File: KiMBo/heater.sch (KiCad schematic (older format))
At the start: 61 parts, among them Q10 2N7002, Q11 2N7002, Q12 DMP3098L-7, Q13 DMP3098L-7, Q4 2N7002, Q5 IPD90P03P4-04, Q6 2N7002, Q7 2N7002, Q8 DMP3098L-7, Q9 DMP3098L-7

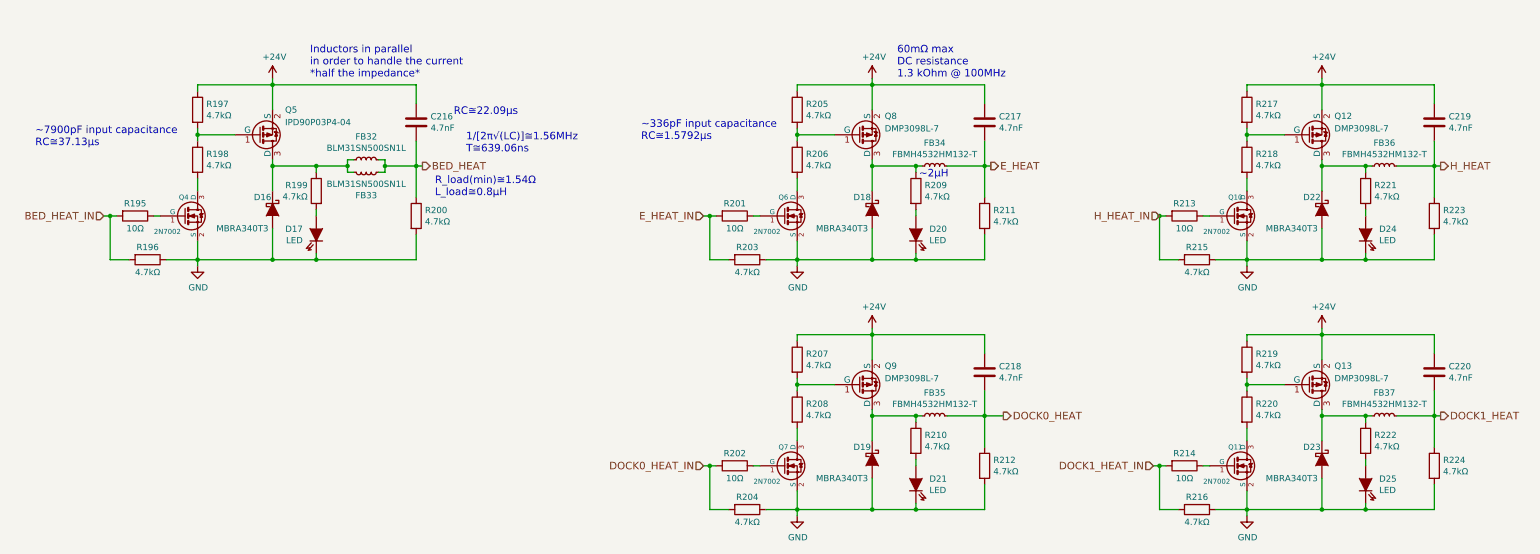
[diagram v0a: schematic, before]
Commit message: Connect X and Z stepper driver open-drain DIAG0 and DIAG1 lines together
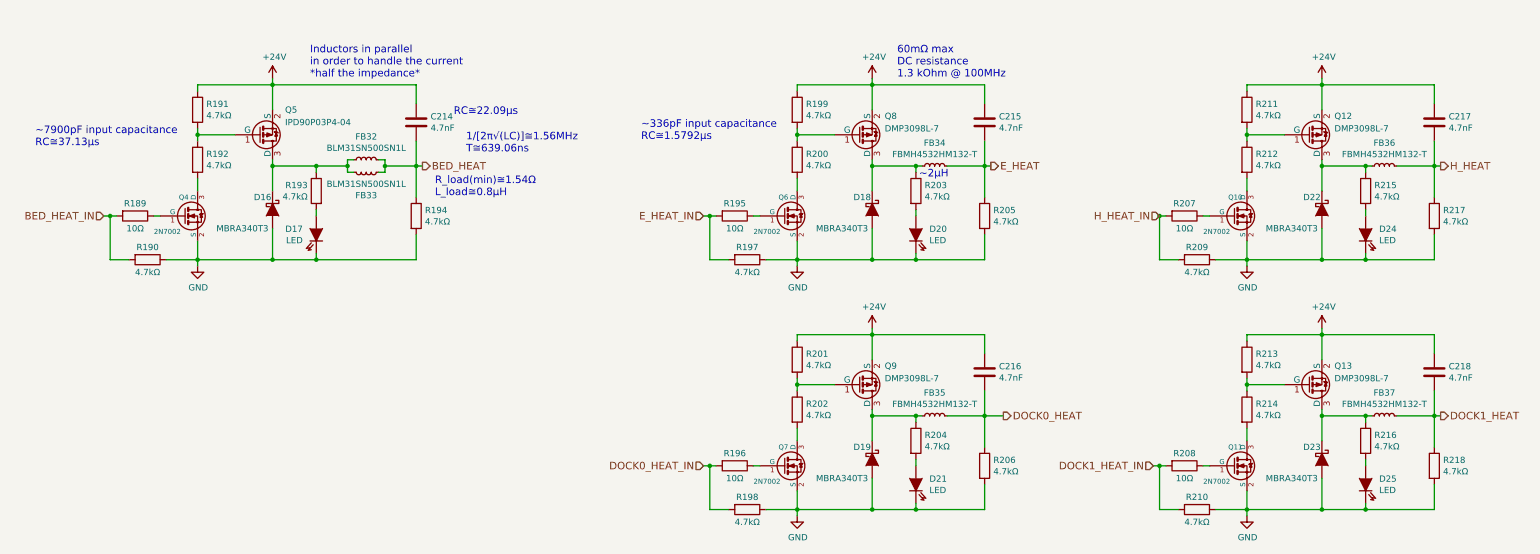
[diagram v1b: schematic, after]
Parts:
- renumbered C216 to C214, C217 to C215, C218 to C216, C219 to C217, C220 to C218, R195 to R189, R196 to R190, R197 to R191, R198 to R192, R199 to R193, R200 to R194, R201 to R195, R202 to R196, R203 to R197, R204 to R198, R205 to R199, R206 to R200, R207 to R201, R208 to R202, R209 to R203, R210 to R204, R211 to R205, R212 to R206, R213 to R207, R214 to R208, R215 to R209, R216 to R210, R217 to R211, R218 to R212, R219 to R213, R220 to R214, R221 to R215, R222 to R216, R223 to R217, R224 to R218

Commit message: Leave SPI0 free for a display, reassign pins so SPI1 is available
Fix some typos/errors
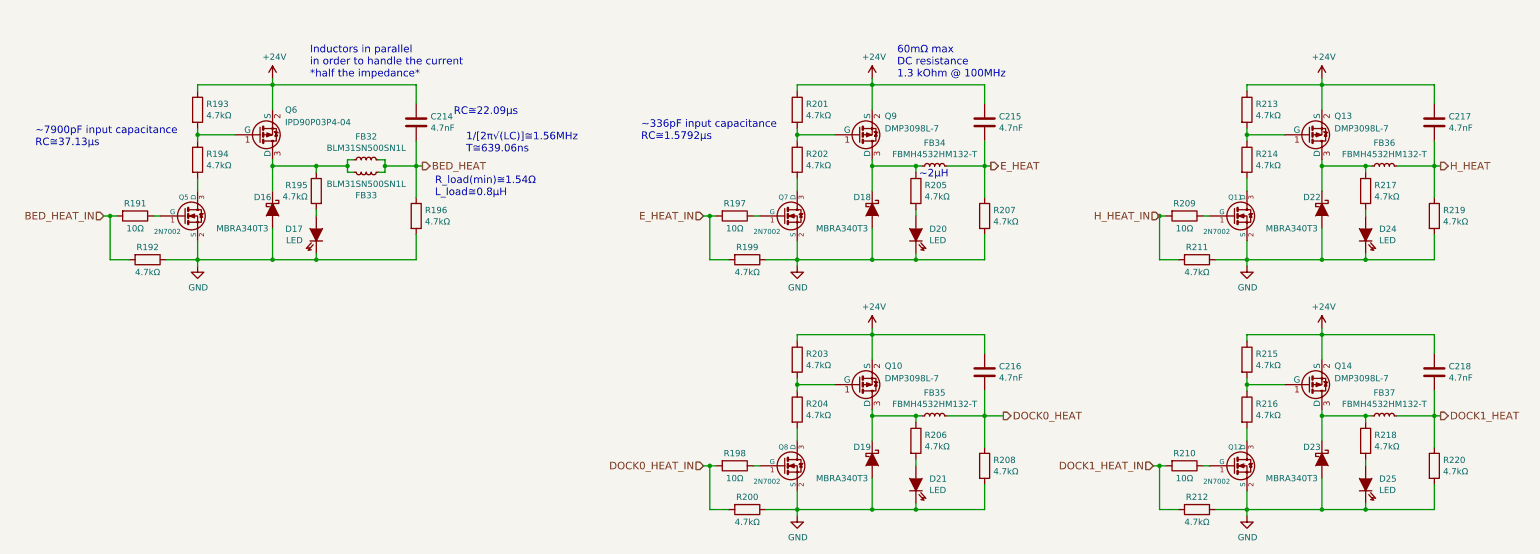
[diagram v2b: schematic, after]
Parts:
- renumbered Q9 to Q10, Q10 to Q11, Q11 to Q12, Q12 to Q13, Q13 to Q14, Q4 to Q5, Q5 to Q6, Q6 to Q7, Q7 to Q8, Q8 to Q9, R189 to R191, R190 to R192, R191 to R193, R192 to R194, R193 to R195, R194 to R196, R195 to R197, R196 to R198, R197 to R199, R198 to R200, R199 to R201, R200 to R202, R201 to R203, R202 to R204, R203 to R205, R204 to R206, R205 to R207, R206 to R208, R207 to R209, R208 to R210, R209 to R211, R210 to R212, R211 to R213, R212 to R214, R213 to R215, R214 to R216, R215 to R217, R216 to R218, R217 to R219, R218 to R220

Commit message: Use fixed 5V LM2592HV Buck, include SPI0 header for LCD
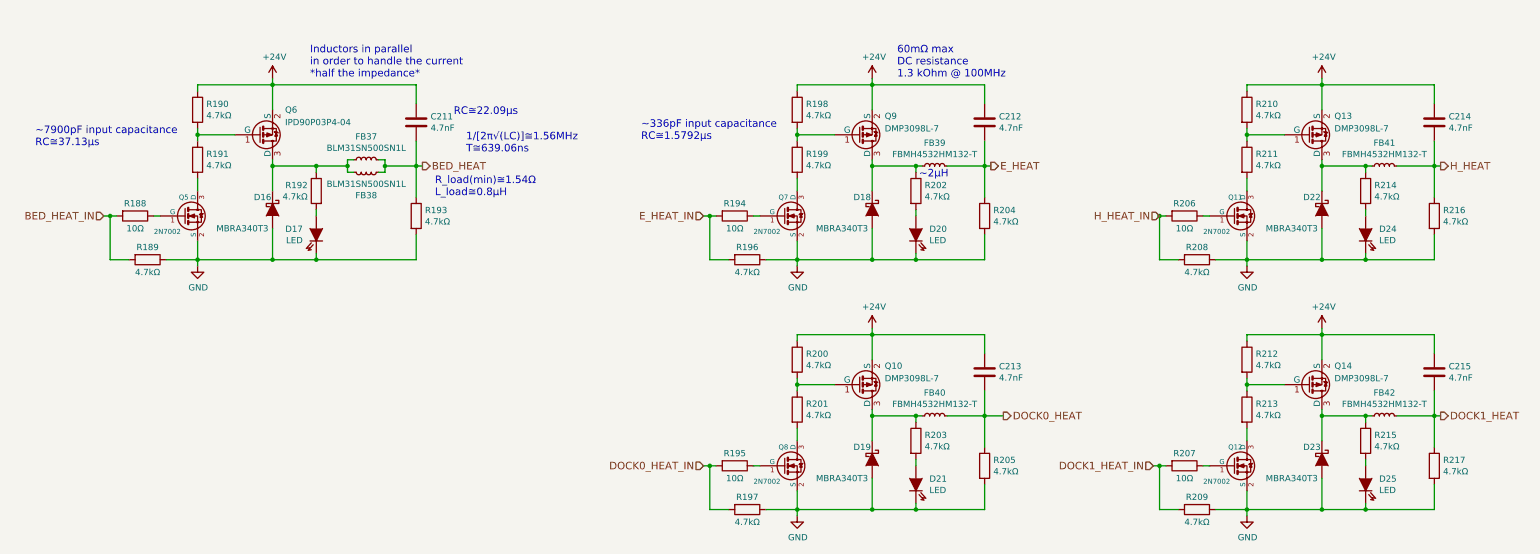
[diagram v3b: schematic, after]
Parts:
- renumbered C214 to C211, C215 to C212, C216 to C213, C217 to C214, C218 to C215, FB32 to FB37, FB33 to FB38, FB34 to FB39, FB35 to FB40, FB36 to FB41, FB37 to FB42, R191 to R188, R192 to R189, R193 to R190, R194 to R191, R195 to R192, R196 to R193, R197 to R194, R198 to R195, R199 to R196, R200 to R197, R201 to R198, R202 to R199, R203 to R200, R204 to R201, R205 to R202, R206 to R203, R207 to R204, R208 to R205, R209 to R206, R210 to R207, R211 to R208, R212 to R209, R213 to R210, R214 to R211, R215 to R212, R216 to R213, R217 to R214, R218 to R215, R219 to R216, R220 to R217

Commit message: Assocate more footprints
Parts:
- C211, C212, C213, C214, C215: footprint Capacitors_SMD:C_0402 -> Capacitors_SMD:C_0603
- D18: renamed from D17; footprint (none) -> LEDs:LED_0603
- D21: renamed from D20; footprint (none) -> LEDs:LED_0603
- D22: renamed from D21; footprint (none) -> LEDs:LED_0603
- D25: renamed from D24; footprint (none) -> LEDs:LED_0603
- D26: renamed from D25; footprint (none) -> LEDs:LED_0603
- FB37, FB38: footprint (none) -> Resistors_SMD:R_1206_HandSoldering
- FB39, FB40, FB41, FB42: footprint (none) -> KiMBo:Ferrite_Bead_1812
- R188, R189, R190, R191, R192, R193, R194, R195, R196, R197, R198, R199, R200, R201, R202, R203, R204, R205, R206, R207, R208, R209, R210, R211, R212, R213, R214, R215, R216, R217: footprint (none) -> Resistors_SMD:R_0603
- renumbered D16 to D17, D18 to D19, D19 to D20, D22 to D23, D23 to D24
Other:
- note added: "refer to\nlanding pattern!"

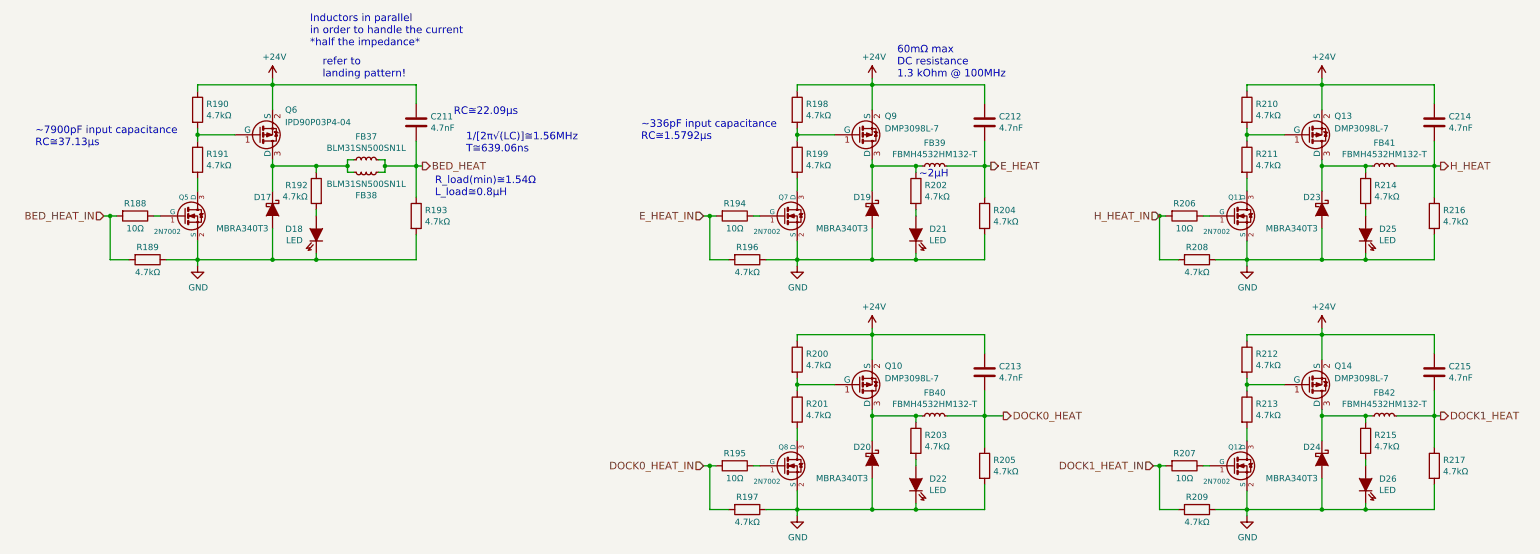
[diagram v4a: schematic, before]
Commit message: More footprint association
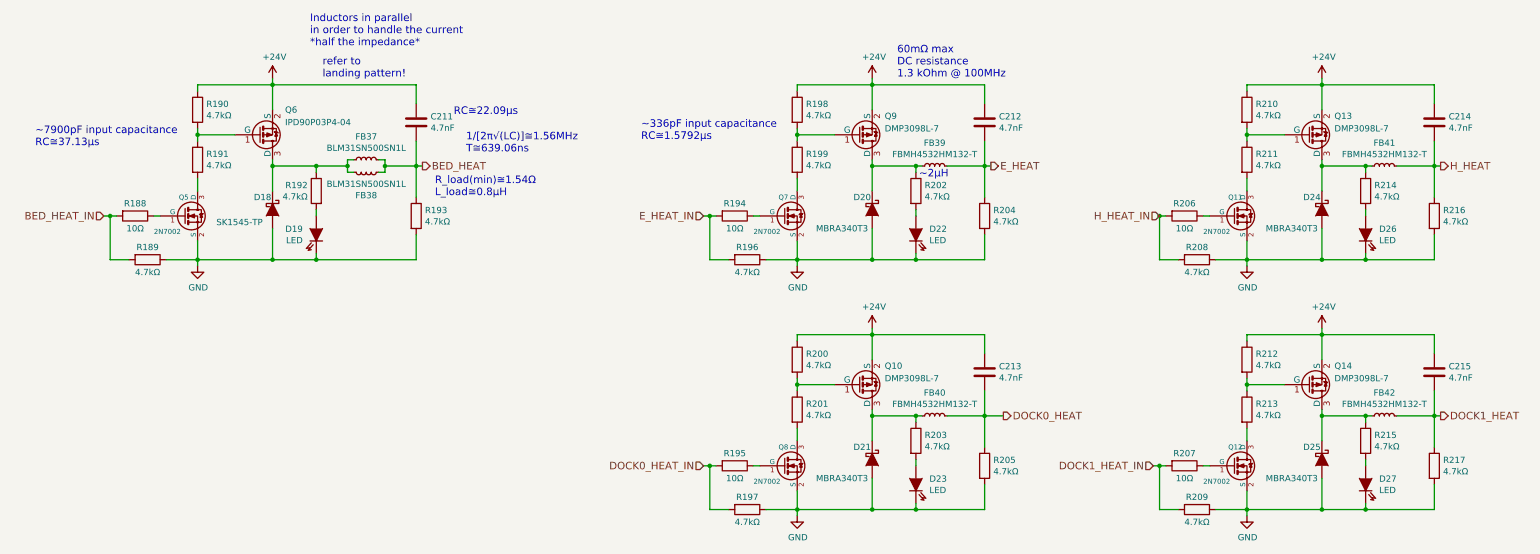
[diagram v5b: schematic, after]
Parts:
- D18: renamed from D17; value MBRA340T3 -> SK1545-TP; footprint (none) -> KiMBo:SK-DO-214AB
- D20: renamed from D19; footprint (none) -> KiMBo:MBR-DO-214AC
- D21: renamed from D20; footprint (none) -> KiMBo:MBR-DO-214AC
- D24: renamed from D23; footprint (none) -> KiMBo:MBR-DO-214AC
- D25: renamed from D24; footprint (none) -> KiMBo:MBR-DO-214AC
- Q10, Q11, Q12, Q13, Q14, Q5, Q7, Q8, Q9: footprint (none) -> TO_SOT_Packages_SMD:SOT-23
- Q6: footprint (none) -> TO_SOT_Packages_SMD:TO-252-2Lead
- renumbered D18 to D19, D21 to D22, D22 to D23, D25 to D26, D26 to D27
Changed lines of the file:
@@
 E_HEAT_IN
 $Comp
-L +24V #PWR0262
+L +24V #PWR0263
 U 1 1 57AD0A58
 P 8350 4350
-F 0 "#PWR0262" H 8350 4200 50  0001 C CNN
+F 0 "#PWR0263" H 8350 4200 50  0001 C CNN
 F 1 "+24V" H 8365 4523 50  0000 C CNN
 F 2 "" H 8350 4350 50  0000 C CNN
@@
 $EndComp
 $Comp
-L GND #PWR0263
+L GND #PWR0264
 U 1 1 57AD222C
 P 7750 5850
-F 0 "#PWR0263" H 7750 5600 50  0001 C CNN
+F 0 "#PWR0264" H 7750 5600 50  0001 C CNN
 F 1 "GND" H 7755 5677 50  0000 C CNN
 F 2 "" H 7750 5850 50  0000 C CNN
@@
 $EndComp
 $Comp
-L D_Schottky D19
+L D_Schottky D20
 U 1 1 57AE0DBA
 P 8350 5400
-F 0 "D19" V 8250 5250 50  0000 L CNN
+F 0 "D20" V 8250 5250 50  0000 L CNN
 F 1 "MBRA340T3" V 8500 4950 50  0000 L CNN
-F 2 "" H 8350 5400 50  0001 C CNN
+F 2 "KiMBo:MBR-DO-214AC" H 8350 5400 50  0001 C CNN
 F 3 "" H 8350 5400 50  0000 C CNN
 	1    8350 5400
@@
 F 0 "Q9" H 8450 4950 50  0000 L CNN
 F 1 "DMP3098L-7" H 8450 4850 50  0000 L CNN
-F 2 "" H 8500 4875 50  0001 L CNN
+F 2 "TO_SOT_Packages_SMD:SOT-23" H 8500 4875 50  0001 L CNN
 F 3 "http://www.diodes.com/_files/datasheets/ds31447.pdf" H 8441 4709 50  0001 L CNN
 	1    8250 4800
@@
 $EndComp
 $Comp
-L GND #PWR0264
+L GND #PWR0265
 U 1 1 57AF39EC
 P 2950 5850
-F 0 "#PWR0264" H 2950 5600 50  0001 C CNN
+F 0 "#PWR0265" H 2950 5600 50  0001 C CNN
 F 1 "GND" H 2955 5677 50  0000 C CNN
 F 2 "" H 2950 5850 50  0000 C CNN
@@
 $EndComp
 $Comp
-L D_Schottky D17
+L D_Schottky D18
 U 1 1 57AF3A03
 P 3550 5400
-F 0 "D17" V 3450 5250 50  0000 L CNN
-F 1 "MBRA340T3" V 3700 4950 50  0000 L CNN
-F 2 "" H 3550 5400 50  0001 C CNN
+F 0 "D18" V 3450 5250 50  0000 L CNN
+F 1 "SK1545-TP" V 3650 4950 50  0000 L CNN
+F 2 "KiMBo:SK-DO-214AB" H 3550 5400 50  0001 C CNN
 F 3 "" H 3550 5400 50  0000 C CNN
 	1    3550 5400
@@
 F 0 "Q6" H 3650 5000 50  0000 L CNN
 F 1 "IPD90P03P4-04" H 3650 4900 50  0000 L CNN
-F 2 "" H 3700 4875 50  0001 L CNN
+F 2 "TO_SOT_Packages_SMD:TO-252-2Lead" H 3700 4875 50  0001 L CNN
 F 3 "http://aosmd.com/res/data_sheets/AOD417.pdf" H 3641 4709 50  0001 L CNN
 	1    3450 4800
@@
 H_HEAT_IN
 $Comp
-L +24V #PWR0265
+L +24V #PWR0266
 U 1 1 57AFEA0C
 P 11950 4350
-F 0 "#PWR0265" H 11950 4200 50  0001 C CNN
+F 0 "#PWR0266" H 11950 4200 50  0001 C CNN
 F 1 "+24V" H 11965 4523 50  0000 C CNN
 F 2 "" H 11950 4350 50  0000 C CNN
@@
 $EndComp
 $Comp
-L GND #PWR0266
+L GND #PWR0267
 U 1 1 57AFEA28
 P 11350 5850
-F 0 "#PWR0266" H 11350 5600 50  0001 C CNN
+F 0 "#PWR0267" H 11350 5600 50  0001 C CNN
 F 1 "GND" H 11355 5677 50  0000 C CNN
 F 2 "" H 11350 5850 50  0000 C CNN
@@
 $EndComp
 $Comp
-L D_Schottky D23
+L D_Schottky D24
 U 1 1 57AFEA3C
 P 11950 5400
-F 0 "D23" V 11850 5250 50  0000 L CNN
+F 0 "D24" V 11850 5250 50  0000 L CNN
 F 1 "MBRA340T3" V 12100 4950 50  0000 L CNN
-F 2 "" H 11950 5400 50  0001 C CNN
+F 2 "KiMBo:MBR-DO-214AC" H 11950 5400 50  0001 C CNN
 F 3 "" H 11950 5400 50  0000 C CNN
 	1    11950 5400
@@
 H_HEAT
 $Comp
-L LED_Short D18
+L LED_Short D19
 U 1 1 59526A10
 P 3900 5600
-F 0 "D18" V 3946 5492 50  0000 R CNN
+F 0 "D19" V 3946 5492 50  0000 R CNN
 F 1 "LED" V 3855 5492 50  0000 R CNN
 F 2 "LEDs:LED_0603" H 3900 5600 50  0001 C CNN
@@
 $EndComp
 $Comp
-L LED_Short D21
+L LED_Short D22
 U 1 1 59526BFD
 P 8700 5600
-F 0 "D21" V 8746 5492 50  0000 R CNN
+F 0 "D22" V 8746 5492 50  0000 R CNN
 F 1 "LED" V 8655 5492 50  0000 R CNN
 F 2 "LEDs:LED_0603" H 8700 5600 50  0001 C CNN
@@
 $EndComp
 $Comp
-L LED_Short D25
+L LED_Short D26
 U 1 1 59526F25
 P 12300 5600
-F 0 "D25" V 12346 5492 50  0000 R CNN
+F 0 "D26" V 12346 5492 50  0000 R CNN
 F 1 "LED" V 12255 5492 50  0000 R CNN
 F 2 "LEDs:LED_0603" H 12300 5600 50  0001 C CNN
@@
 DOCK0_HEAT_IN
 $Comp
-L +24V #PWR0267
+L +24V #PWR0268
 U 1 1 59DB237A
 P 8350 6350
-F 0 "#PWR0267" H 8350 6200 50  0001 C CNN
+F 0 "#PWR0268" H 8350 6200 50  0001 C CNN
 F 1 "+24V" H 8365 6523 50  0000 C CNN
 F 2 "" H 8350 6350 50  0000 C CNN
@@
 $EndComp
 $Comp
-L GND #PWR0268
+L GND #PWR0269
 U 1 1 59DB2387
 P 7750 7850
-F 0 "#PWR0268" H 7750 7600 50  0001 C CNN
+F 0 "#PWR0269" H 7750 7600 50  0001 C CNN
 F 1 "GND" H 7755 7677 50  0000 C CNN
 F 2 "" H 7750 7850 50  0000 C CNN
@@
 $EndComp
 $Comp
-L D_Schottky D20
+L D_Schottky D21
 U 1 1 59DB2394
 P 8350 7400
-F 0 "D20" V 8250 7250 50  0000 L CNN
+F 0 "D21" V 8250 7250 50  0000 L CNN
 F 1 "MBRA340T3" V 8500 6950 50  0000 L CNN
-F 2 "" H 8350 7400 50  0001 C CNN
+F 2 "KiMBo:MBR-DO-214AC" H 8350 7400 50  0001 C CNN
 F 3 "" H 8350 7400 50  0000 C CNN
 	1    8350 7400
@@
 DOCK1_HEAT_IN
 $Comp
-L +24V #PWR0269
+L +24V #PWR0270
 U 1 1 59DB23D2
 P 11950 6350
-F 0 "#PWR0269" H 11950 6200 50  0001 C CNN
+F 0 "#PWR0270" H 11950 6200 50  0001 C CNN
 F 1 "+24V" H 11965 6523 50  0000 C CNN
 F 2 "" H 11950 6350 50  0000 C CNN
@@
 $EndComp
 $Comp
-L GND #PWR0270
+L GND #PWR0271
 U 1 1 59DB23DF
 P 11350 7850
-F 0 "#PWR0270" H 11350 7600 50  0001 C CNN
+F 0 "#PWR0271" H 11350 7600 50  0001 C CNN
 F 1 "GND" H 11355 7677 50  0000 C CNN
 F 2 "" H 11350 7850 50  0000 C CNN
@@
 $EndComp
 $Comp
-L D_Schottky D24
+L D_Schottky D25
 U 1 1 59DB23EC
 P 11950 7400
-F 0 "D24" V 11850 7250 50  0000 L CNN
+F 0 "D25" V 11850 7250 50  0000 L CNN
 F 1 "MBRA340T3" V 12100 6950 50  0000 L CNN
-F 2 "" H 11950 7400 50  0001 C CNN
+F 2 "KiMBo:MBR-DO-214AC" H 11950 7400 50  0001 C CNN
 F 3 "" H 11950 7400 50  0000 C CNN
 	1    11950 7400
@@
 DOCK1_HEAT
 $Comp
-L LED_Short D22
+L LED_Short D23
 U 1 1 59DB2439
 P 8700 7600
-F 0 "D22" V 8746 7492 50  0000 R CNN
+F 0 "D23" V 8746 7492 50  0000 R CNN
 F 1 "LED" V 8655 7492 50  0000 R CNN
 F 2 "LEDs:LED_0603" H 8700 7600 50  0001 C CNN
@@
 $EndComp
 $Comp
-L LED_Short D26
+L LED_Short D27
 U 1 1 59DB2440
 P 12300 7600
-F 0 "D26" V 12346 7492 50  0000 R CNN
+F 0 "D27" V 12346 7492 50  0000 R CNN
 F 1 "LED" V 12255 7492 50  0000 R CNN
 F 2 "LEDs:LED_0603" H 12300 7600 50  0001 C CNN
@@
 $EndComp
 $Comp
-L +24V #PWR0271
+L +24V #PWR0272
 U 1 1 5B13B3A2
 P 3550 4350
-F 0 "#PWR0271" H 3550 4200 50  0001 C CNN
+F 0 "#PWR0272" H 3550 4200 50  0001 C CNN
 F 1 "+24V" H 3565 4523 50  0000 C CNN
 F 2 "" H 3550 4350 50  0000 C CNN
@@
 F 0 "Q10" H 8450 6950 50  0000 L CNN
 F 1 "DMP3098L-7" H 8450 6850 50  0000 L CNN
-F 2 "" H 8500 6875 50  0001 L CNN
+F 2 "TO_SOT_Packages_SMD:SOT-23" H 8500 6875 50  0001 L CNN
 F 3 "http://www.diodes.com/_files/datasheets/ds31447.pdf" H 8441 6709 50  0001 L CNN
 	1    8250 6800
@@
 F 0 "Q13" H 12050 4950 50  0000 L CNN
 F 1 "DMP3098L-7" H 12050 4850 50  0000 L CNN
-F 2 "" H 12100 4875 50  0001 L CNN
+F 2 "TO_SOT_Packages_SMD:SOT-23" H 12100 4875 50  0001 L CNN
 F 3 "http://www.diodes.com/_files/datasheets/ds31447.pdf" H 12041 4709 50  0001 L CNN
 	1    11850 4800
@@
 F 0 "Q14" H 12050 6950 50  0000 L CNN
 F 1 "DMP3098L-7" H 12050 6850 50  0000 L CNN
-F 2 "" H 12100 6875 50  0001 L CNN
+F 2 "TO_SOT_Packages_SMD:SOT-23" H 12100 6875 50  0001 L CNN
 F 3 "http://www.diodes.com/_files/datasheets/ds31447.pdf" H 12041 6709 50  0001 L CNN
 	1    11850 6800
@@
 F 0 "Q5" H 2800 5600 40  0000 L CNN
 F 1 "2N7002" H 2600 5325 40  0000 L CNN
-F 2 "" H 2720 5552 29  0001 C CNN
+F 2 "TO_SOT_Packages_SMD:SOT-23" H 2720 5552 29  0001 C CNN
 F 3 "" H 2850 5450 60  0000 C CNN
 	1    2850 5450
@@
 F 0 "Q7" H 7600 5600 40  0000 L CNN
 F 1 "2N7002" H 7400 5325 40  0000 L CNN
-F 2 "" H 7520 5552 29  0001 C CNN
+F 2 "TO_SOT_Packages_SMD:SOT-23" H 7520 5552 29  0001 C CNN
 F 3 "" H 7650 5450 60  0000 C CNN
 	1    7650 5450
@@
 F 0 "Q11" H 11200 5600 40  0000 L CNN
 F 1 "2N7002" H 11000 5325 40  0000 L CNN
-F 2 "" H 11120 5552 29  0001 C CNN
+F 2 "TO_SOT_Packages_SMD:SOT-23" H 11120 5552 29  0001 C CNN
 F 3 "" H 11250 5450 60  0000 C CNN
 	1    11250 5450
@@
 F 0 "Q12" H 11200 7600 40  0000 L CNN
 F 1 "2N7002" H 11000 7325 40  0000 L CNN
-F 2 "" H 11120 7552 29  0001 C CNN
+F 2 "TO_SOT_Packages_SMD:SOT-23" H 11120 7552 29  0001 C CNN
 F 3 "" H 11250 7450 60  0000 C CNN
 	1    11250 7450
@@
 F 0 "Q8" H 7600 7600 40  0000 L CNN
 F 1 "2N7002" H 7400 7325 40  0000 L CNN
-F 2 "" H 7520 7552 29  0001 C CNN
+F 2 "TO_SOT_Packages_SMD:SOT-23" H 7520 7552 29  0001 C CNN
 F 3 "" H 7650 7450 60  0000 C CNN
 	1    7650 7450
